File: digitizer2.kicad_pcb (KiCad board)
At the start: 6 copper layers, 4 parts, among them U1 XC7A35T, U2 FT2232H, U3 MT41J128M16, U4 ADS5403

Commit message: DRAM tuned
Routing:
- net /DRAM_BA0: track 22.8 -> 35.6 mm
- net /DRAM_A7: track 24.7 -> 35.6 mm
- net /DRAM_A3: track 24.8 -> 35.6 mm
- net /DRAM_WE: track 25.4 -> 35.8 mm
- net /DRAM_A0: track 25.4 -> 35.6 mm
- net /DRAM_ODT: track 25.9 -> 35.5 mm
- net /DRAM_A2: track 26.1 -> 35.6 mm
- net /DRAM_A13: track 26.4 -> 35.7 mm
- net /DRAM_A9: track 27.7 -> 35.7 mm
- net /DRAM_A5: track 28.0 -> 35.6 mm
- net /DRAM_BA2: track 28.6 -> 35.7 mm
- net /DRAM_A6: track 29.2 -> 35.6 mm
- net /DRAM_A8: track 30.5 -> 35.6 mm
- net /DRAM_RAS: track 31.1 -> 35.6 mm
- net /DRAM_CAS: track 31.2 -> 35.6 mm
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
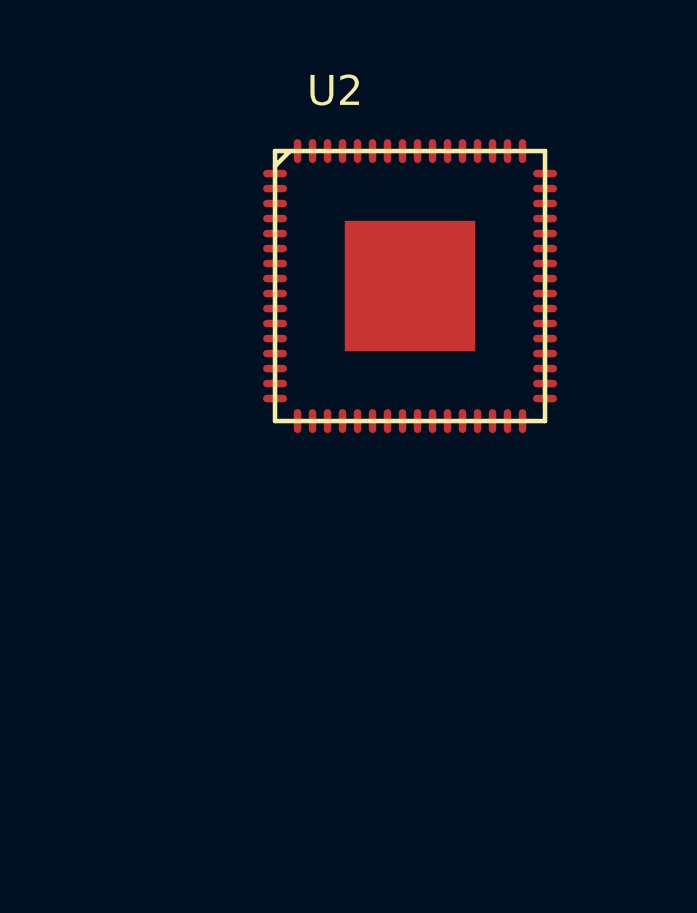
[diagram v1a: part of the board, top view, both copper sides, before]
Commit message: Realign FTDI
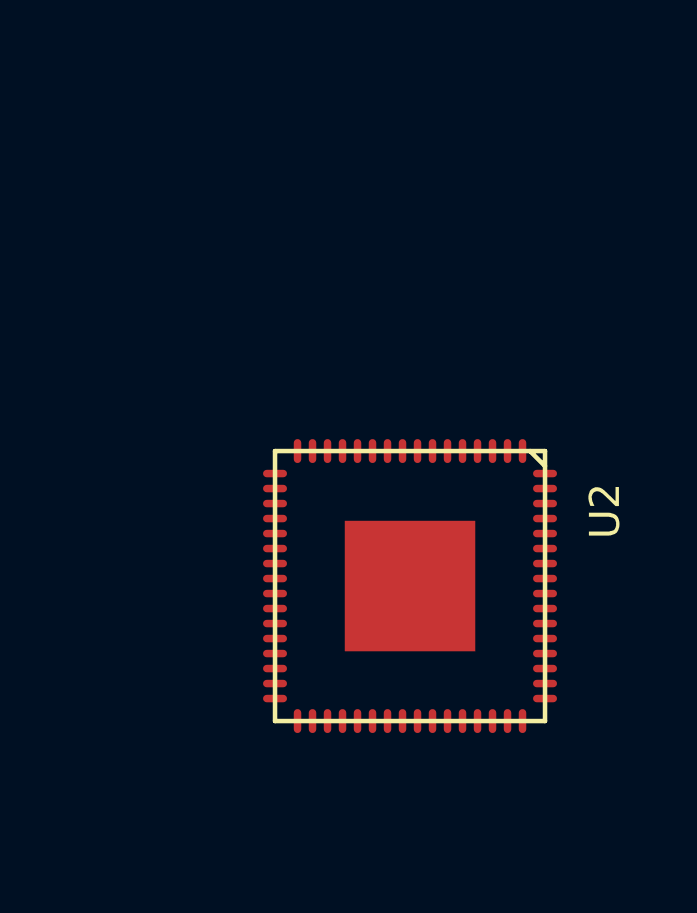
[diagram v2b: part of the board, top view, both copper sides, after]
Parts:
- moved U2 10.0 mm to (190.0, 70.0), turned to 270 degrees

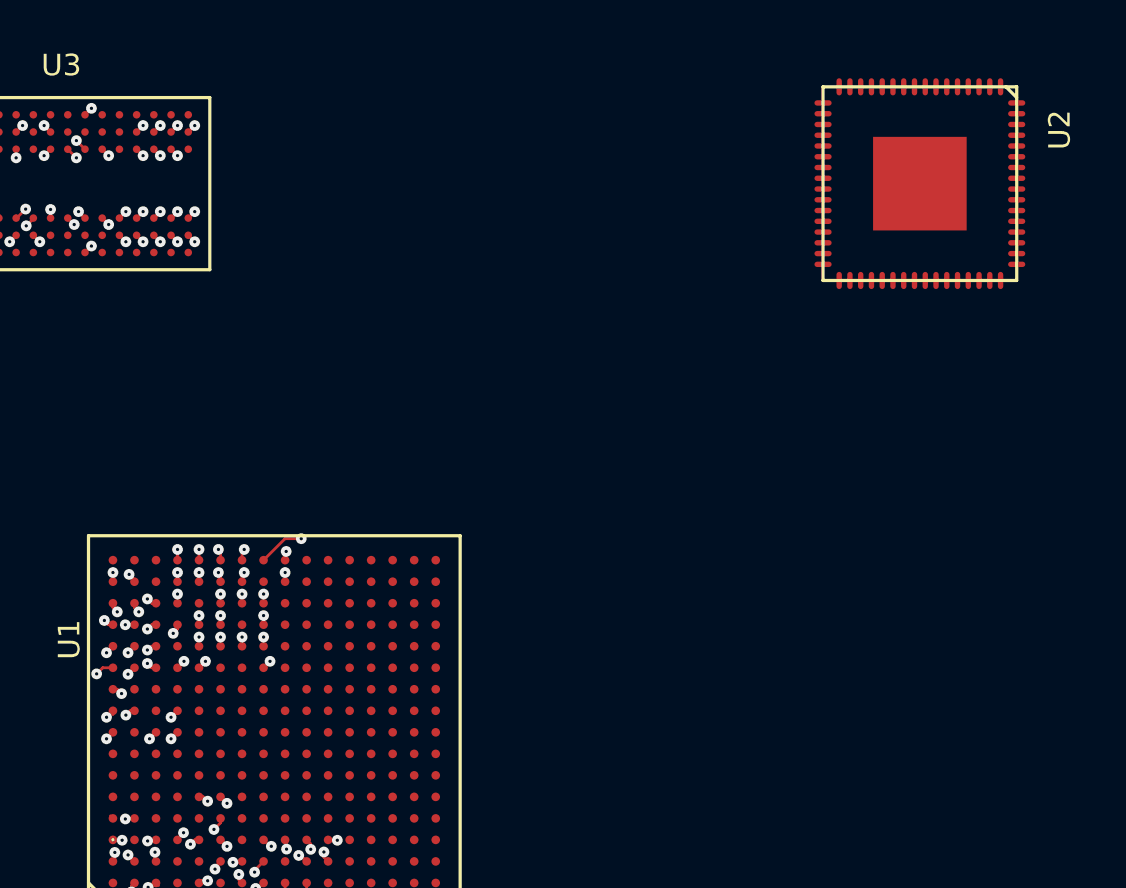
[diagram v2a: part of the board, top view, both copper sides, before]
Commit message: Layout FTDI interface
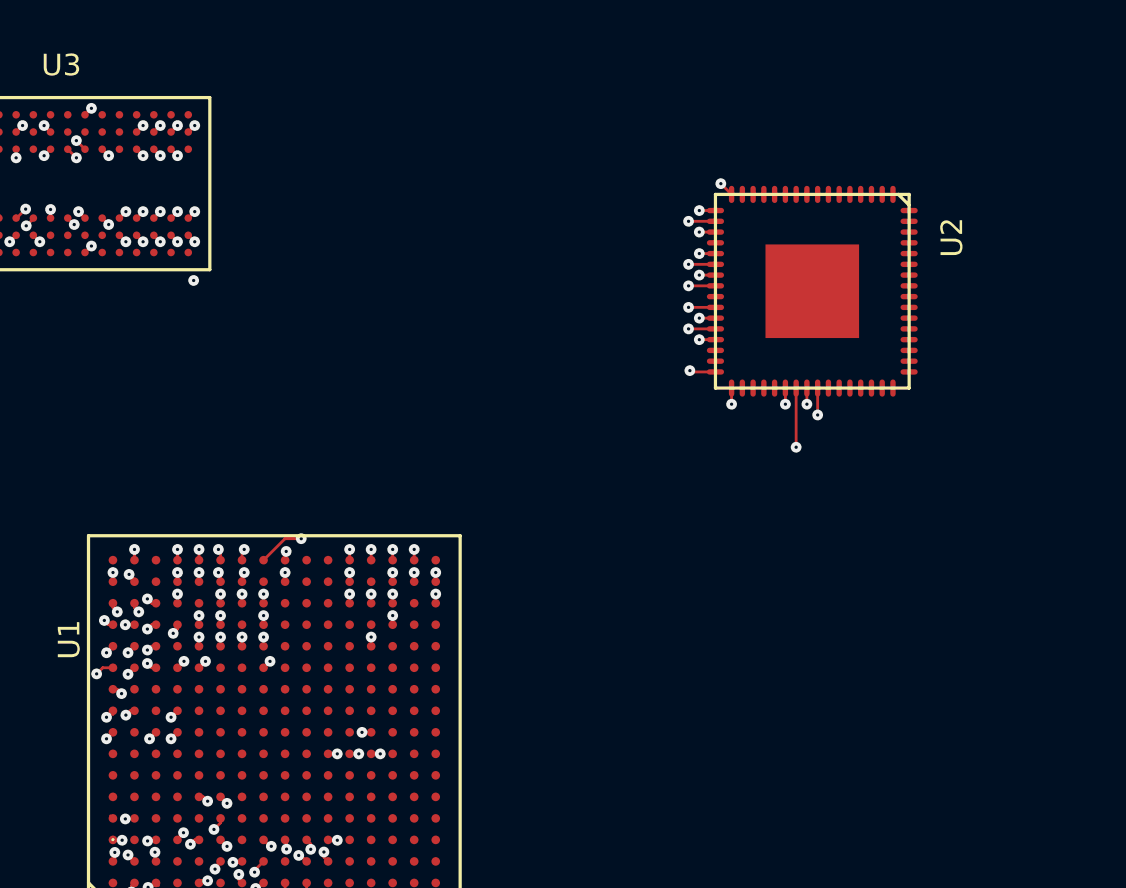
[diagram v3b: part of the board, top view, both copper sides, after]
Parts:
- moved U2 7.07 mm to (185.0, 75.0)
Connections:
- net Net-(U4-PadB12) renamed /ADC_RESET
- U1 pad M14: Net-(U1-PadM14) -> /USB_RXF
- U1 pad M15: Net-(U1-PadM15) -> /USB_D1
- U1 pad M16: Net-(U1-PadM16) -> /USB_D0
- U1 pad N12: Net-(U1-PadN12) -> /USB_CLKOUT
- U1 pad N14: Net-(U1-PadN14) -> /USB_D3
- U1 pad N16: Net-(U1-PadN16) -> /USB_D2
- U1 pad P13: Net-(U1-PadP13) -> /USB_OE
- U1 pad P14: Net-(U1-PadP14) -> /USB_TXE
- U1 pad P15: Net-(U1-PadP15) -> /USB_D5
- U1 pad P16: Net-(U1-PadP16) -> /USB_D4
- U1 pad R15: Net-(U1-PadR15) -> /USB_D7
- U1 pad R16: Net-(U1-PadR16) -> /USB_D6
- U1 pad T14: Net-(U1-PadT14) -> /USB_WR
- U1 pad T15: Net-(U1-PadT15) -> /USB_RD
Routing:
- net /DRAM_RESET: track 0.42 -> 35.6 mm, vias 1 -> 3
- net /JTAG_TMS: track 0.00 -> 30.0 mm, vias 0 -> 2
- net /JTAG_TCK: track 0.00 -> 29.6 mm, vias 0 -> 2
- net /JTAG_TDI: track 0.00 -> 28.8 mm, vias 0 -> 2
- net /JTAG_TDO: track 0.00 -> 28.6 mm, vias 0 -> 2
- net /USB_D6: track 0.00 -> 28.1 mm, vias 0 -> 2
- net /USB_D2: track 0.00 -> 28.1 mm, vias 0 -> 2
- net /USB_RXF: track 0.00 -> 28.1 mm, vias 0 -> 2
- net /USB_D4: track 0.00 -> 28.1 mm, vias 0 -> 2
- net /USB_RD: track 0.00 -> 28.1 mm, vias 0 -> 2
- net /USB_D7: track 0.00 -> 28.1 mm, vias 0 -> 2
- net /USB_TXE: track 0.00 -> 28.0 mm, vias 0 -> 2
- net /USB_OE: track 0.00 -> 28.0 mm, vias 0 -> 2
- net /USB_WR: track 0.00 -> 28.0 mm, vias 0 -> 2
- net /USB_CLKOUT: track 0.00 -> 28.0 mm, vias 0 -> 2
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
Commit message: Serial interfaces, cleanup
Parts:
- moved U2 4.75 mm to (185.0, 79.8)
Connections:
- net /ADC_SDO renamed Net-(U4-PadA10)
- U1 pad N1: Net-(U1-PadN1) -> /ADC_SDIO
- U1 pad N2: Net-(U1-PadN2) -> /ADC_SRESET
- U1 pad P1: Net-(U1-PadP1) -> /ADC_SCLK
- U1 pad R1: Net-(U1-PadR1) -> /ADC_SDENB
- U4 pad B12: /ADC_RESET -> /ADC_SRESET
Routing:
- net /ADC_SRESET: track 0.00 -> 34.9 mm, vias 0 -> 2
- net /ADC_SDENB: track 0.00 -> 34.8 mm, vias 0 -> 2
- net /ADC_SCLK: track 0.00 -> 34.1 mm, vias 0 -> 2
- net /ADC_SDIO: track 0.00 -> 32.0 mm, vias 0 -> 2
- net /USB_RD: track 28.1 -> 16.1 mm
- net /USB_WR: track 28.0 -> 16.4 mm
- net /USB_OE: track 28.0 -> 19.6 mm
- net /USB_CLKOUT: track 28.0 -> 19.6 mm
- net /USB_D6: track 28.1 -> 23.5 mm
- net /USB_D2: track 28.1 -> 23.5 mm
- net /USB_D4: track 28.1 -> 23.5 mm
- net /USB_TXE: track 28.0 -> 23.5 mm
- net /USB_D7: track 28.1 -> 23.5 mm
- net /USB_RXF: track 28.1 -> 23.5 mm
- net /USB_D1: track 28.0 -> 23.5 mm
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
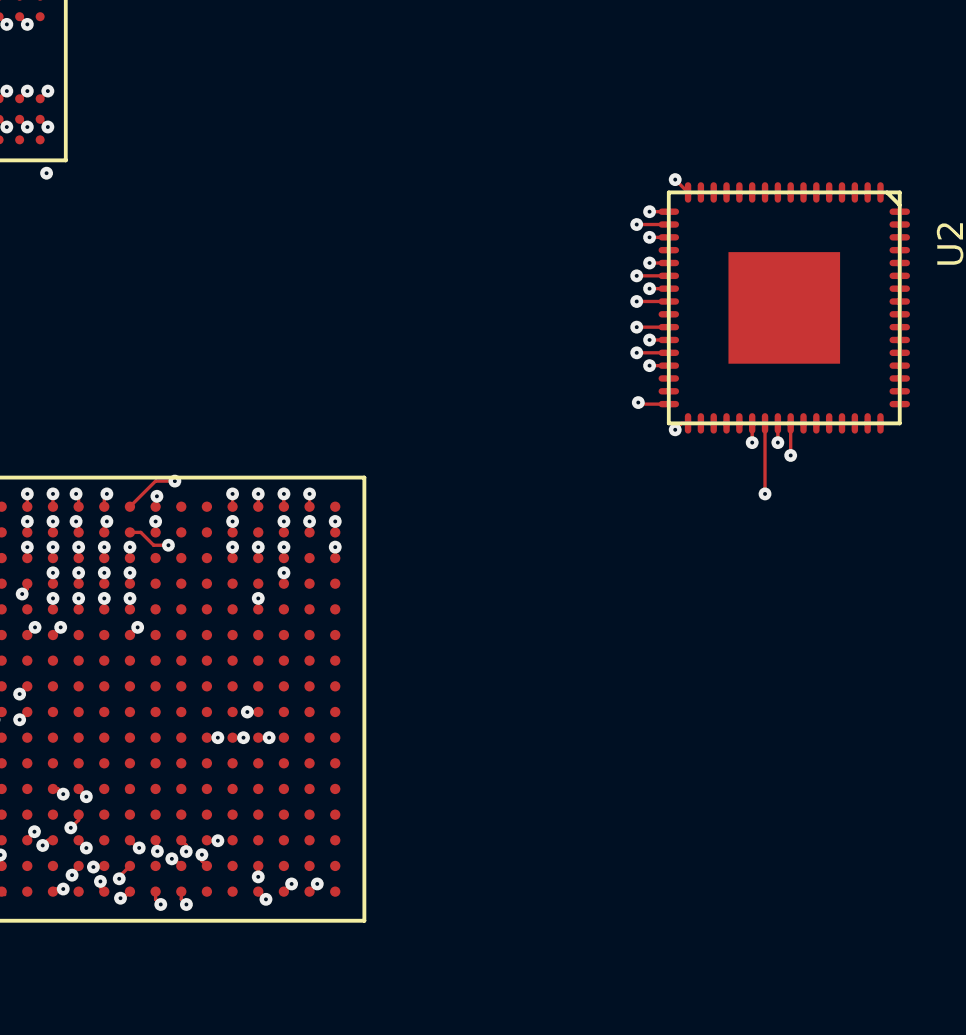
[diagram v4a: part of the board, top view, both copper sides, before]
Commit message: Add ADC evaluation board documents, add usb tracks
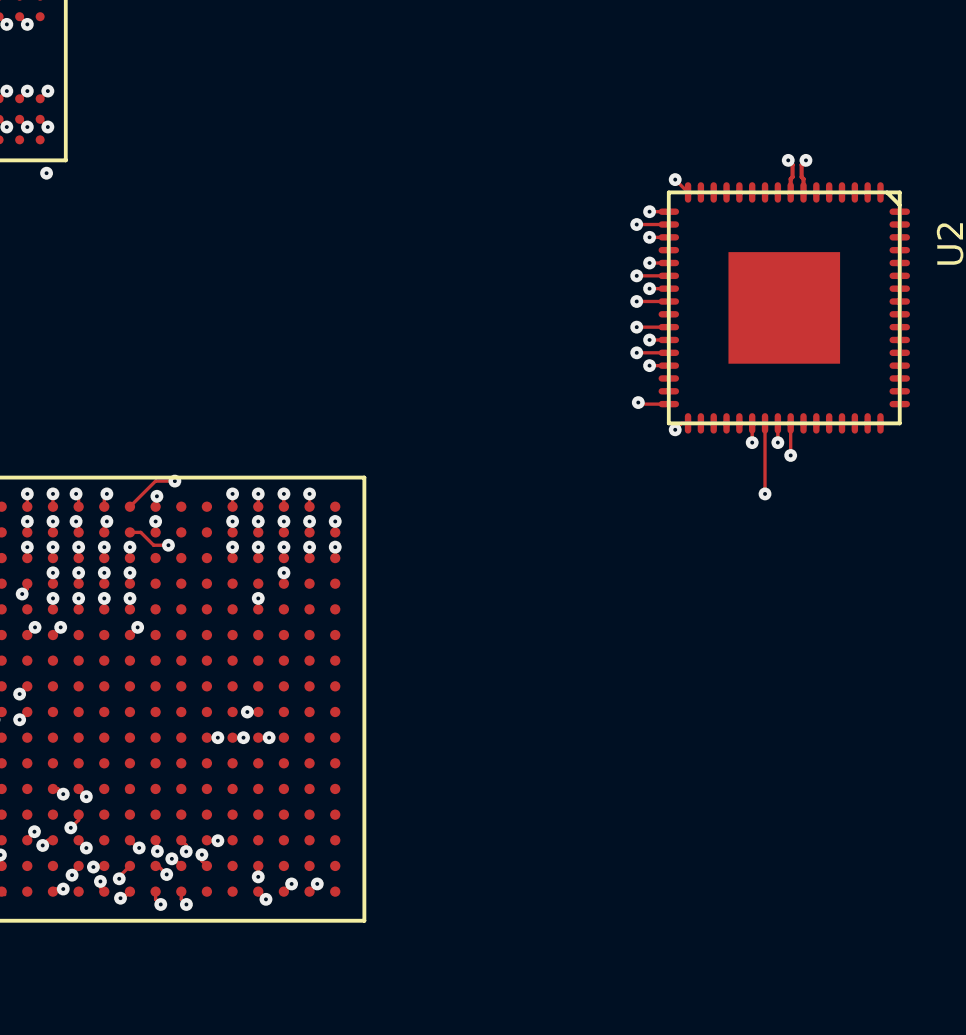
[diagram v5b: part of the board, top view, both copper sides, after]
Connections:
- net /USB_CON_DM renamed /USB_CON_D_N
- net /USB_CON_DP renamed /USB_CON_D_P
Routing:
- net /USB_CON_D_P: track 0.00 -> 12.2 mm, vias 0 -> 1
- net /USB_CON_D_N: track 0.00 -> 12.2 mm, vias 0 -> 1
- net Net-(U1-PadJ2): track 0.00 -> 0.57 mm, vias 0 -> 1
- net Net-(U1-PadR14): track 0.00 -> 0.43 mm, vias 0 -> 1
- net Net-(U1-PadN15): track 0.00 -> 0.43 mm, vias 0 -> 1
